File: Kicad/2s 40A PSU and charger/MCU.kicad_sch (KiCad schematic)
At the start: 0 parts

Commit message: Reworked PSU to use CH32X035 and USB-PD
This will save a few bucks and will actually be a cooler solution than just a DC jack connected to some pads
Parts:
- added C25: 0.1uF, Capacitor_SMD:C_0402_1005Metric, symbol Device:C_Small
- added C26: 4.7uF, Capacitor_SMD:C_0603_1608Metric, symbol Device:C_Small
- added D4: Osram LT Q99G.01 green led, LED_SMD:LED_0603_1608Metric_Pad1.05x0.95mm_HandSolder, symbol Device:LED
- added J12: USB, Connector_PinHeader_1.27mm:PinHeader_1x02_P1.27mm_Vertical, symbol Connector:Conn_01x02_Socket
- added R11, R29: 10k, Resistor_SMD:R_0402_1005Metric, symbol Device:R_Small
- added R25: 80.6 ohm, Resistor_SMD:R_0402_1005Metric, symbol Device:R_Small
- added R26, R27, R28: 120 ohm, Resistor_SMD:R_0402_1005Metric, symbol Device:R_Small
- added TP1: SWC, TestPoint:TestPoint_Pad_D1.0mm, symbol Connector:TestPoint
- added TP3: ~, TestPoint:TestPoint_Pad_D1.0mm, symbol Connector:TestPoint
- added TP4: SWD, TestPoint:TestPoint_Pad_D1.0mm, symbol Connector:TestPoint
- added U5: THVD1420DRLR, Package_TO_SOT_SMD:SOT-583-8, symbol Interface_UART:THVD1420D
- added U6: CH32X035G8U6, Package_DFN_QFN:QFN-28-1EP_4x4mm_P0.4mm_EP2.6x2.6mm_ThermalVias, symbol wch_mcu:CH32X035G8U6
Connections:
- new net: D4.2 (A), R25.2
- new net 3.3v: C25.1, C26.1, R11.2, R28.1, R29.2, U5.8 (VCC), U6.2 (VDD)
- new net Balancer Alert: U6.14 (PB3)
- new net CC1: U6.28 (CC1/PC14)
- new net CC2: U6.1 (CC2/PC15)
- new net CS: U6.9 (ADC4/PA4)
- new net Charger IADP: U6.5 (ADC0/PA0)
- new net Charger IDCHG: U6.13 (PB0/ADC8)
- new net Charger PROCHOT: U6.15 (PB4)
- new net D+/BOOT: J12.1 (Pin_1), TP3.1, U6.27 (USB1_DP/PC17)
- new net D-: J12.2 (Pin_2), U6.26 (USB1_DM/PC16)
- new net GND: C25.2, C26.2, D4.1 (K), R26.2, U5.2 (~{RE}), U5.5 (GND), U6.29 (GND)
- new net LED: R25.1, U6.16 (PB1/PB5/ADC9)
- new net MISO: U6.11 (ADC6/PA6)
- new net MOSI: U6.12 (ADC7/PA7)
- new net PWRON: U6.17 (PB6)
- new net RS485+: R27.2, R28.2, U5.7 (B)
- new net RS485-: R26.1, R27.1, U5.6 (A)
- new net SCL: R29.1, TP1.1, U6.24 (SWCLK/PC19)
- new net SCLK: U6.10 (ADC5/PA5)
- new net SDA: R11.1, TP4.1, U6.25 (SWDIO/PC18)
- new net UART1-RTS: U5.3 (DE), U6.6 (ADC1/PA1)
- new net UART1_RX: U5.1 (RO), U6.8 (ADC3/PA3)
- new net UART1_TX: U5.4 (DI), U6.7 (ADC2/PA2)
- no-connect marks 0 -> 8
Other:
- note added: "PB1 and PB5 are tied internally"
- note added: "RST does not exist on the QFN28 package"

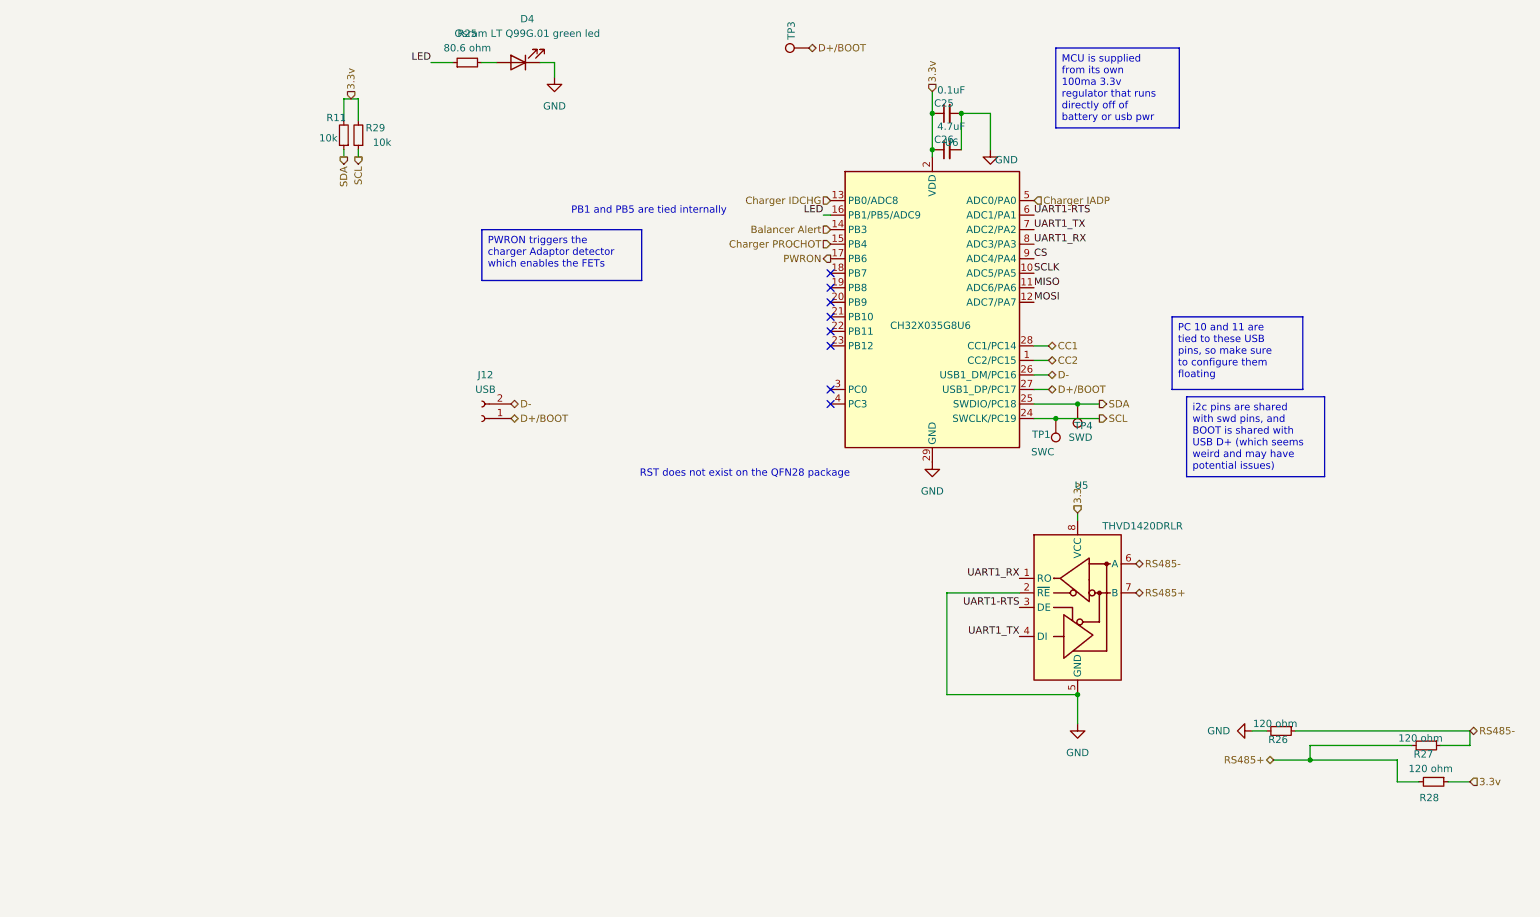
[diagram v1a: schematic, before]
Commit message: Improved schematic formatting and visuals
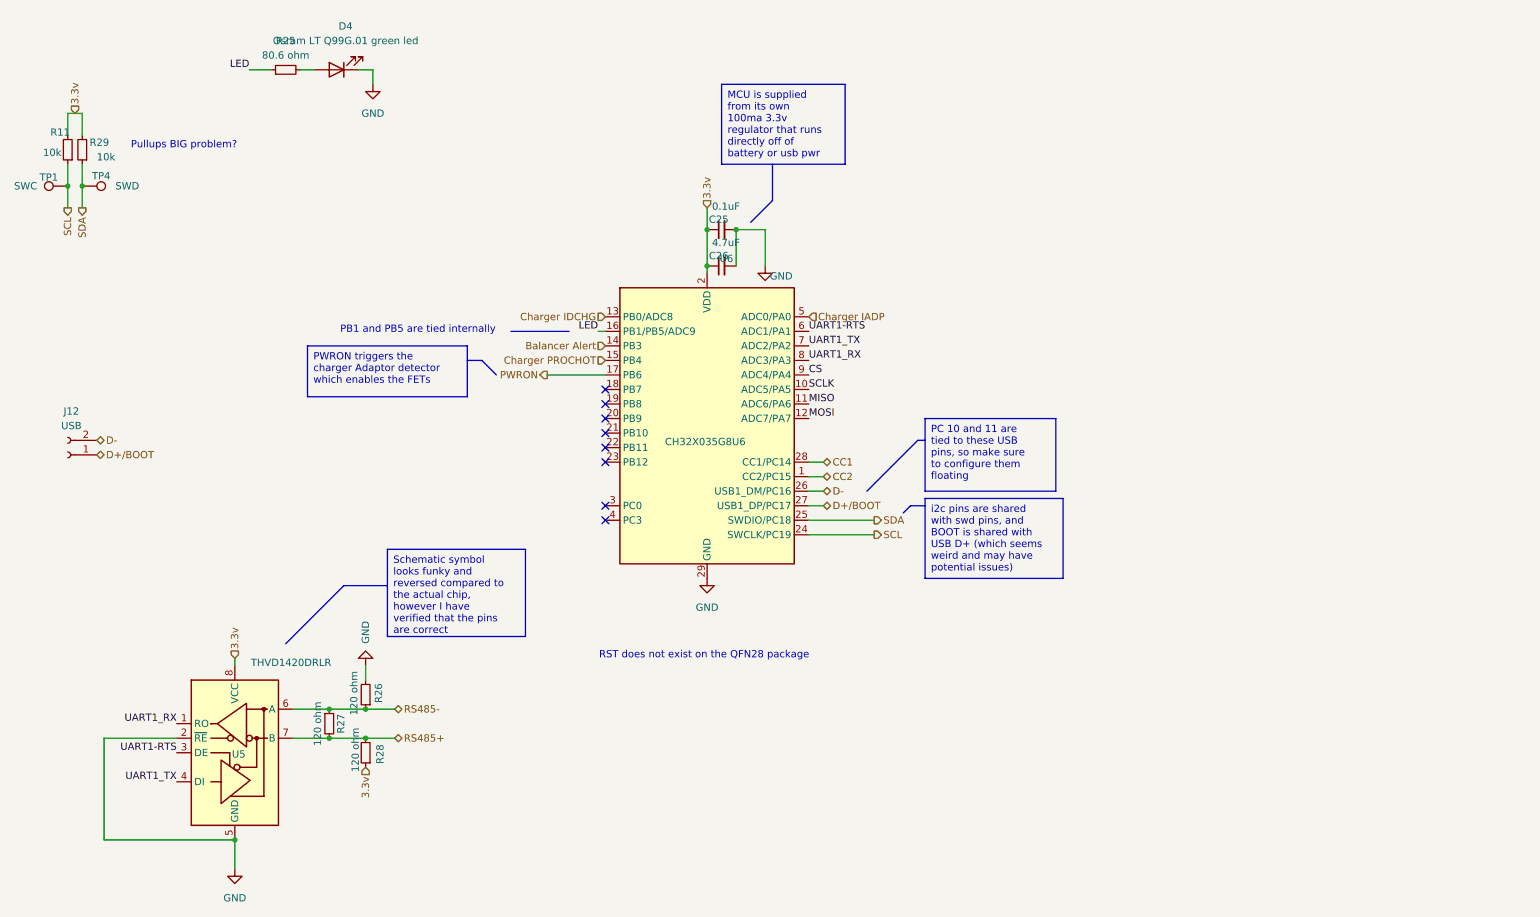
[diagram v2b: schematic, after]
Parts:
- removed TP3: ~, TestPoint:TestPoint_Pad_D1.0mm, symbol Connector:TestPoint
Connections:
- net SCL: now also R11.1; no longer R29.1
- net SDA: now also R29.1; no longer R11.1
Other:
- note added: "Pullups BIG problem?"
- moved on the sheet: C25, C26, D4, J12, R11, R25, R26, R27, R28, R29, TP1, TP4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

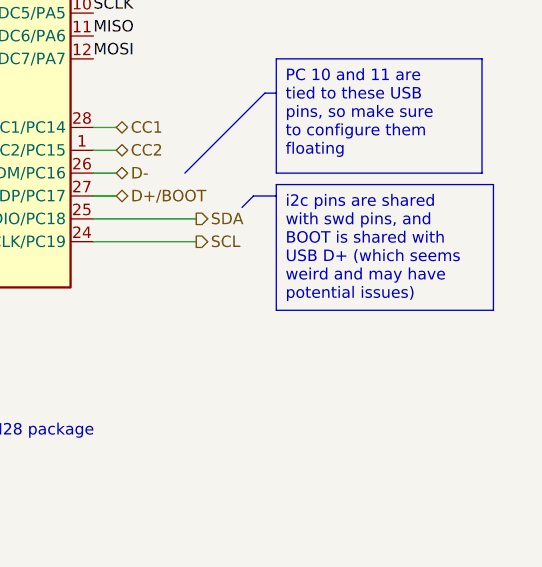
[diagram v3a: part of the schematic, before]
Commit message: Add proper ESD protection and pulldowns for USB-C
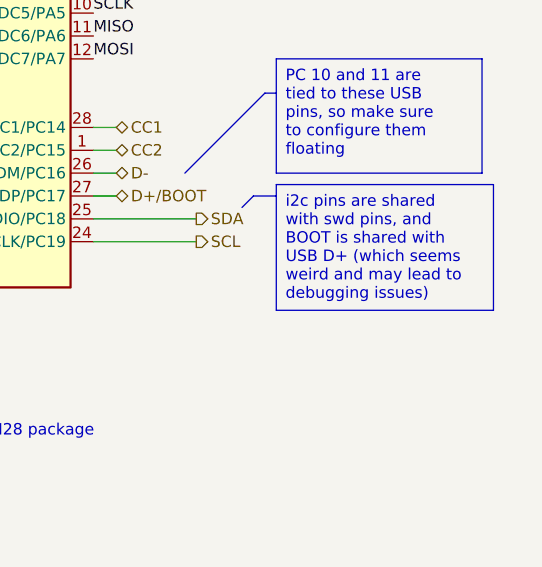
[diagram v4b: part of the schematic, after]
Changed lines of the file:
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@@
 		)
 	)
-	(text_box "i2c pins are shared with swd pins, and BOOT is shared with USB D+ (which seems weird and may have potential issues)"
+	(text_box "i2c pins are shared with swd pins, and BOOT is shared with USB D+ (which seems weird and may lead to debugging issues)"
 		(exclude_from_sim no)
 		(at 179.07 105.41 0)

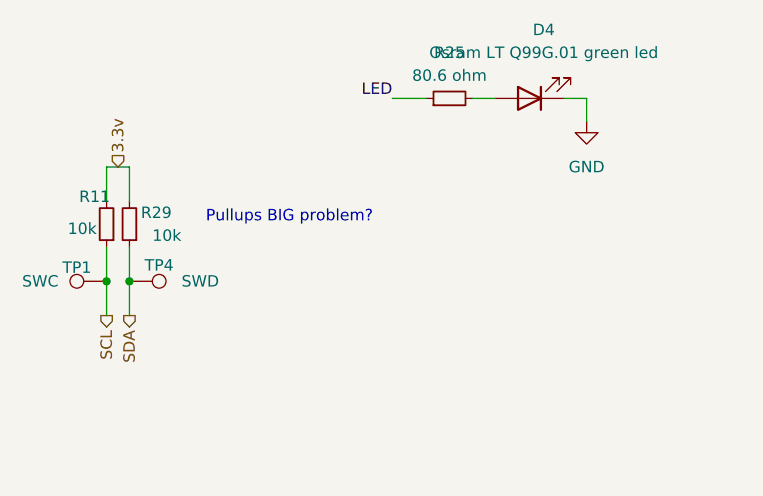
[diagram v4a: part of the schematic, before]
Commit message: Updated Ground connections and tweaked some formatting
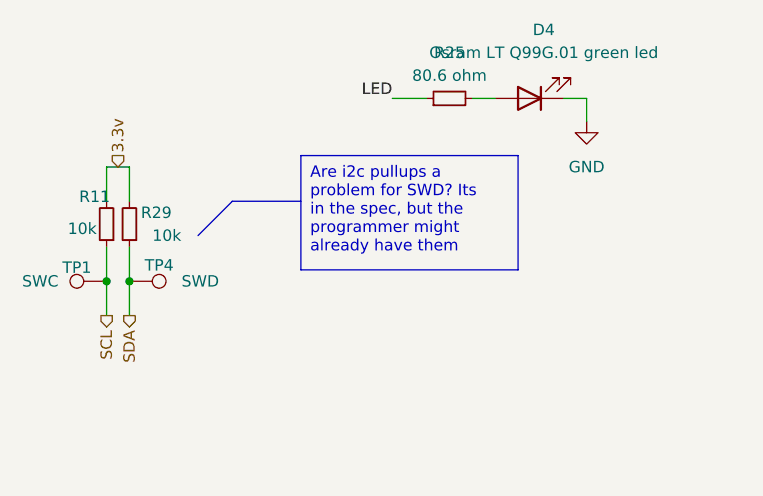
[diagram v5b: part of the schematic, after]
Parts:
- U6: footprint Package_DFN_QFN:QFN-28-1EP_4x4mm_P0.4mm_EP2.6x2.6mm_ThermalVias -> Package_DFN_QFN:QFN-28-1EP_4x4mm_P0.4mm_EP2.8x2.8mm
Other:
- note removed: "Pullups BIG problem?"
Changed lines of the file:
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@@
+		)
+	)
+	(polyline
+		(pts
+			(xy 50.8 41.91) (xy 43.18 41.91)
+		)
+		(stroke
+			(width 0)
+			(type default)
 		)
 	)
@@
 		(pts
 			(xy 35.56 147.32) (xy 35.56 165.1)
+		)
+		(stroke
+			(width 0)
+			(type default)
+		)
+	)
+	(polyline
+		(pts
+			(xy 39.37 45.72) (xy 43.18 41.91)
 		)
 		(stroke
@@
 		)
 	)
-	(text "Pullups BIG problem?"
-		(exclude_from_sim no)
-		(at 49.53 43.688 0)
-		(effects
-			(font
-				(size 1.27 1.27)
-			)
+	(text_box "Are i2c pullups a problem for SWD? Its in the spec, but the programmer might already have them"
+		(exclude_from_sim no)
+		(at 50.8 36.83 0)
+		(size 24.13 12.7)
+		(stroke
+			(width 0)
+			(type default)
+		)
+		(fill
+			(type none)
+		)
+		(effects
+			(font
+				(size 1.27 1.27)
+			)
+			(justify left top)
 		)
 	)
@@
 			)
 		)
-		(property "Footprint" "Package_DFN_QFN:QFN-28-1EP_4x4mm_P0.4mm_EP2.6x2.6mm_ThermalVias"
+		(property "Footprint" "Package_DFN_QFN:QFN-28-1EP_4x4mm_P0.4mm_EP2.8x2.8mm"
 			(at 146.05 142.24 0)
 			(effects

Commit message: Updated Sheet Properties
My author name is now in there, and I've added the proper project name.
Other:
- company: (none) -> ME
- title: (none) -> CACKLE 2s 40A PSU & Charger
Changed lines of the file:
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@@
 	(paper "A4")
 	(title_block
-		(date "2024-11-28")
-		(rev "V1 Alpha")
+		(title "CACKLE 2s 40A PSU & Charger")
+		(date "2024-12-01")
+		(rev "V1")
+		(company "ME")
+		(comment 1 "Author: Asher Edwards")
 	)
 	(junction

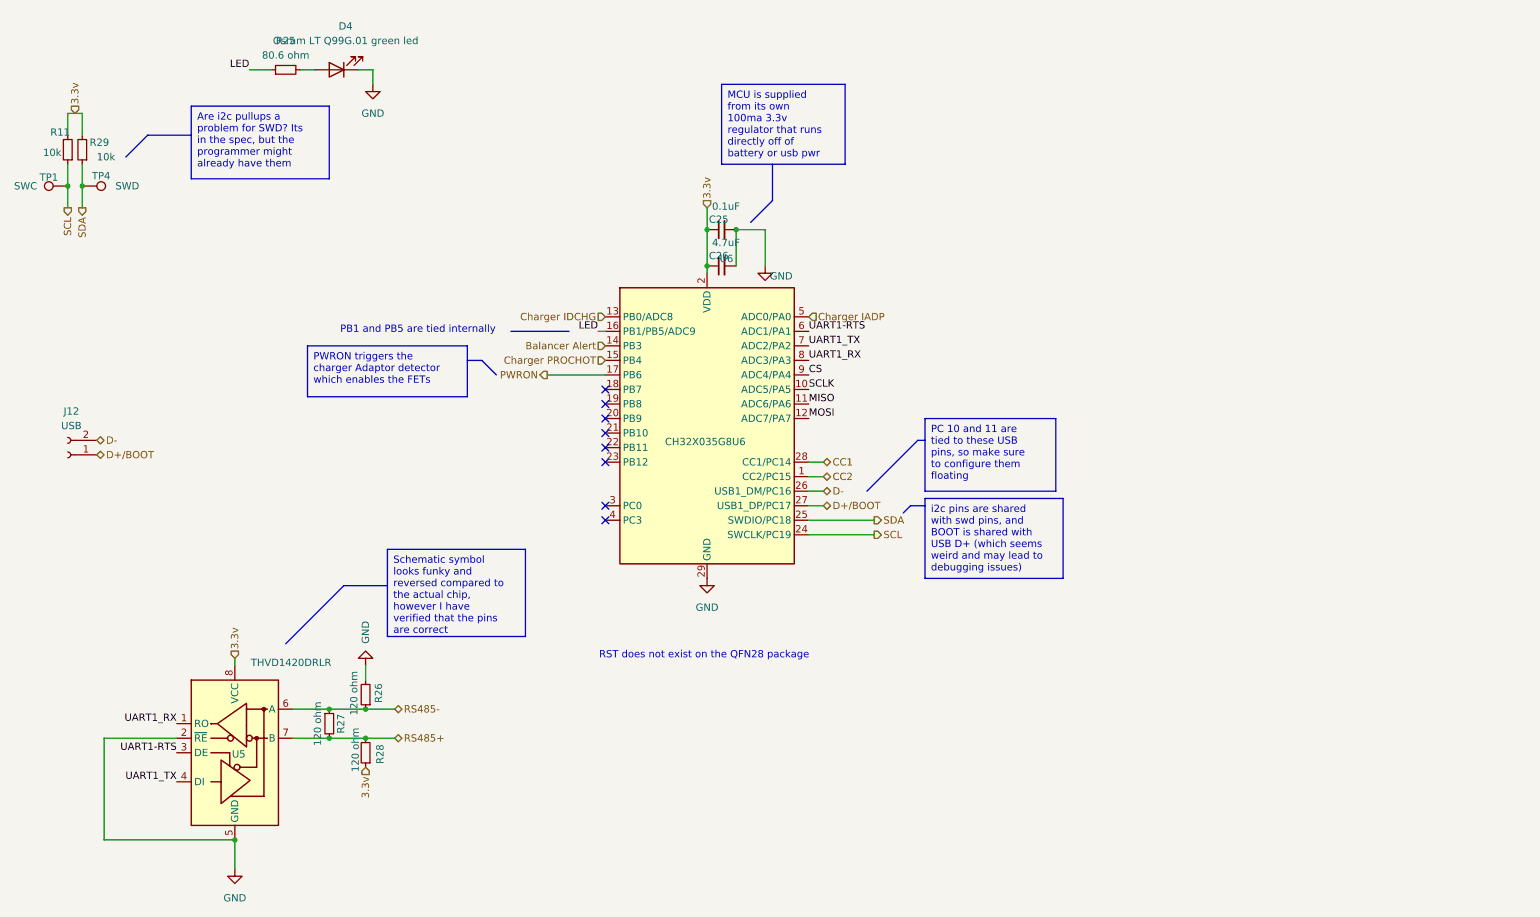
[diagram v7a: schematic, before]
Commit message: Finished Layout of PSU
Gosh, this has taken a long time on and off, almost 2 months!
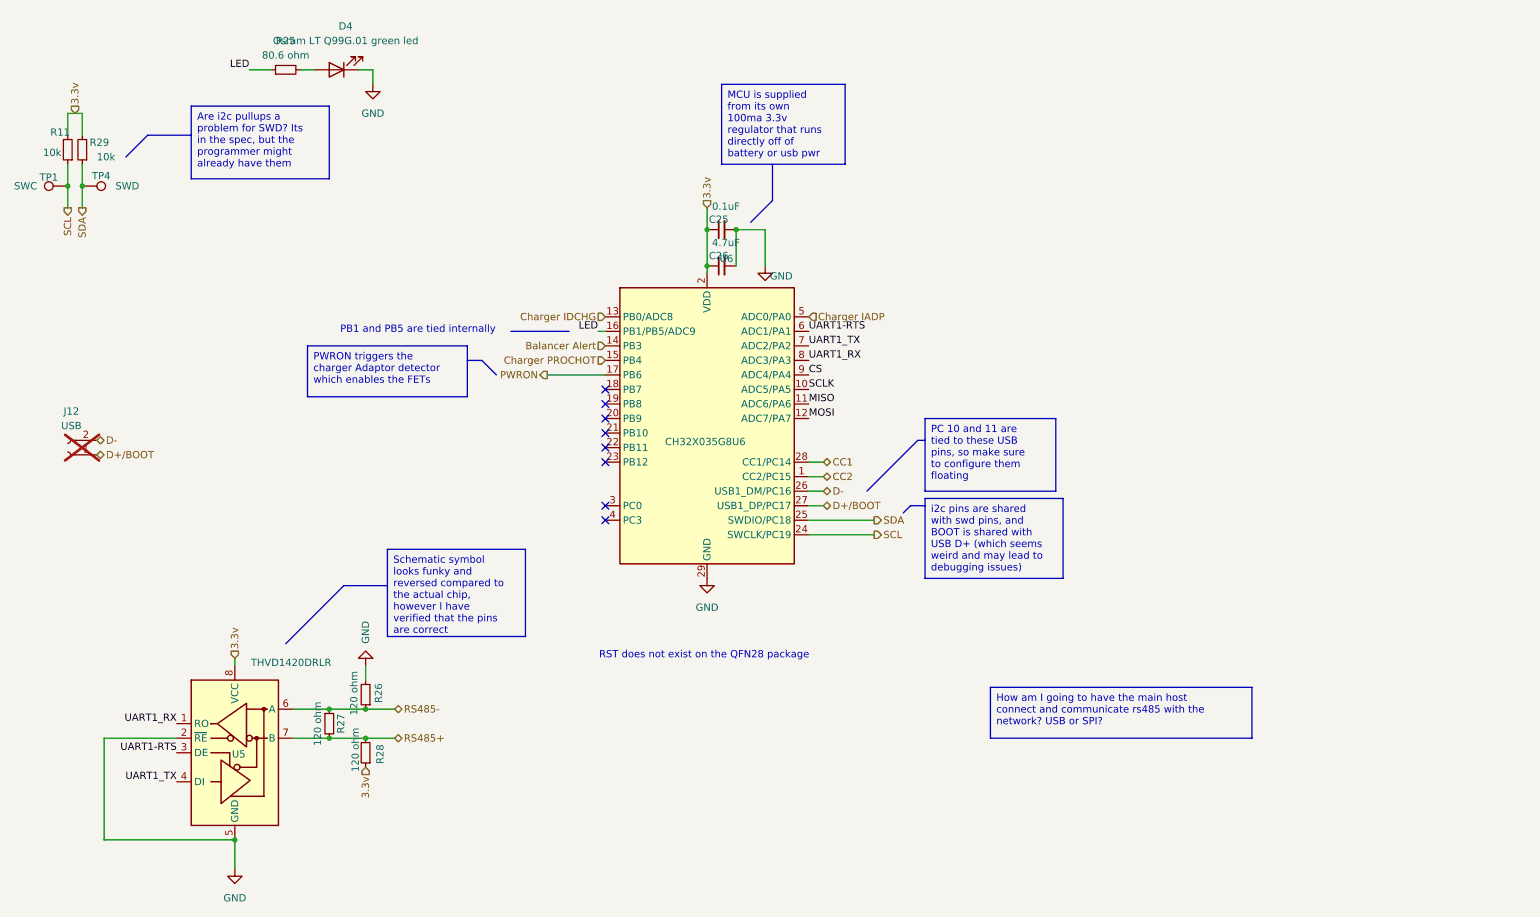
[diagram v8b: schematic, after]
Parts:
- J12: now not fitted; now left out of the parts list
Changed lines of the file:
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@@
+		)
+	)
+	(text_box "How am I going to have the main host connect and communicate rs485 with the network? USB or SPI?"
+		(exclude_from_sim no)
+		(at 190.5 138.43 0)
+		(size 45.72 8.89)
+		(stroke
+			(width 0)
+			(type default)
+		)
+		(fill
+			(type none)
+		)
+		(effects
+			(font
+				(size 1.27 1.27)
+			)
+			(justify left top)
 		)
 	)
@@
 		(unit 1)
 		(exclude_from_sim no)
-		(in_bom yes)
-		(on_board yes)
-		(dnp no)
+		(in_bom no)
+		(on_board yes)
+		(dnp yes)
 		(fields_autoplaced yes)
 		(property "Reference" "J12"
